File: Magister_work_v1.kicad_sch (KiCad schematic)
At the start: 0 parts

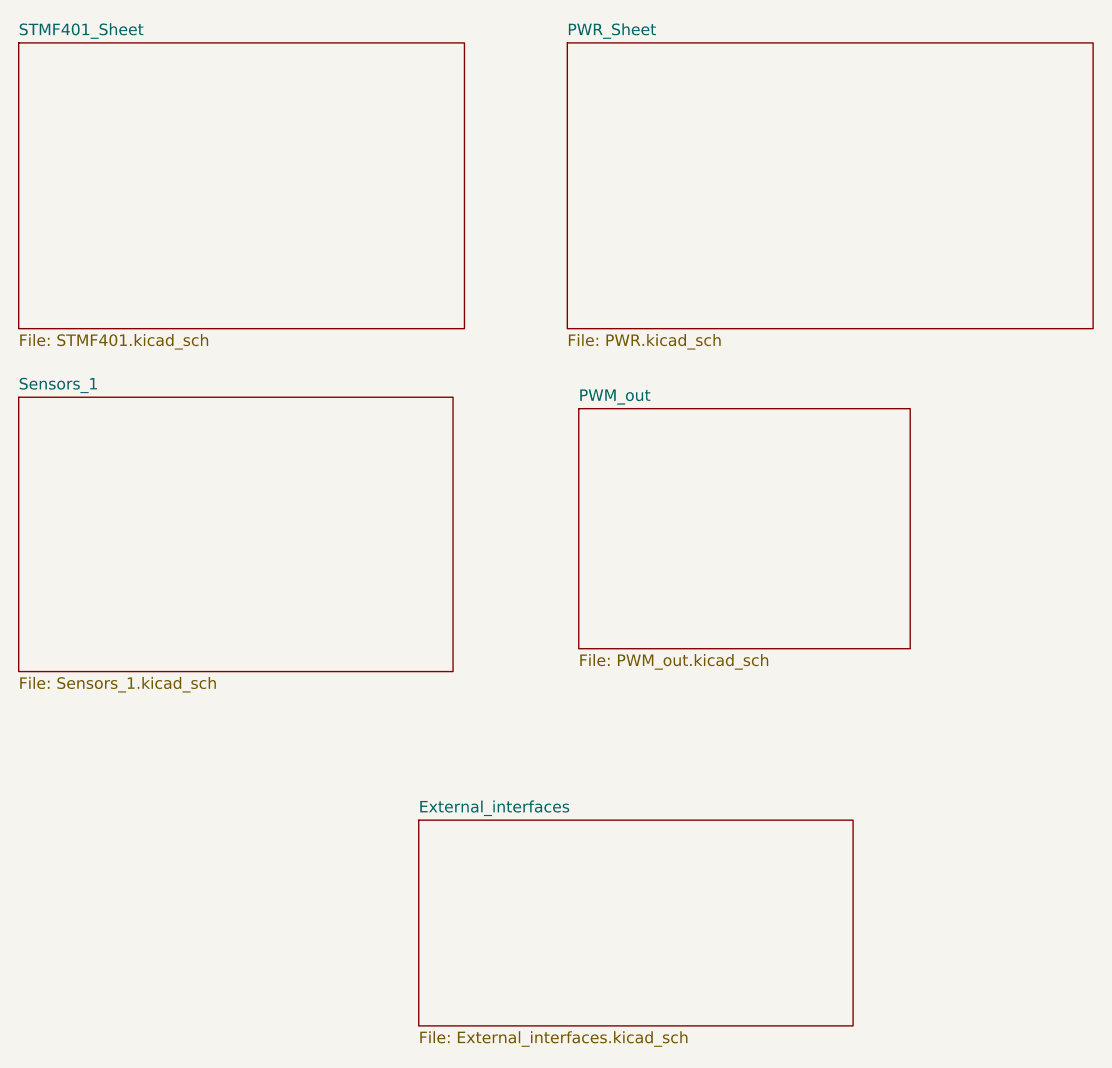
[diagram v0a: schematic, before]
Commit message: feat:убрал часть с батарейным питанием, убрал лишние элементы со старого проекта
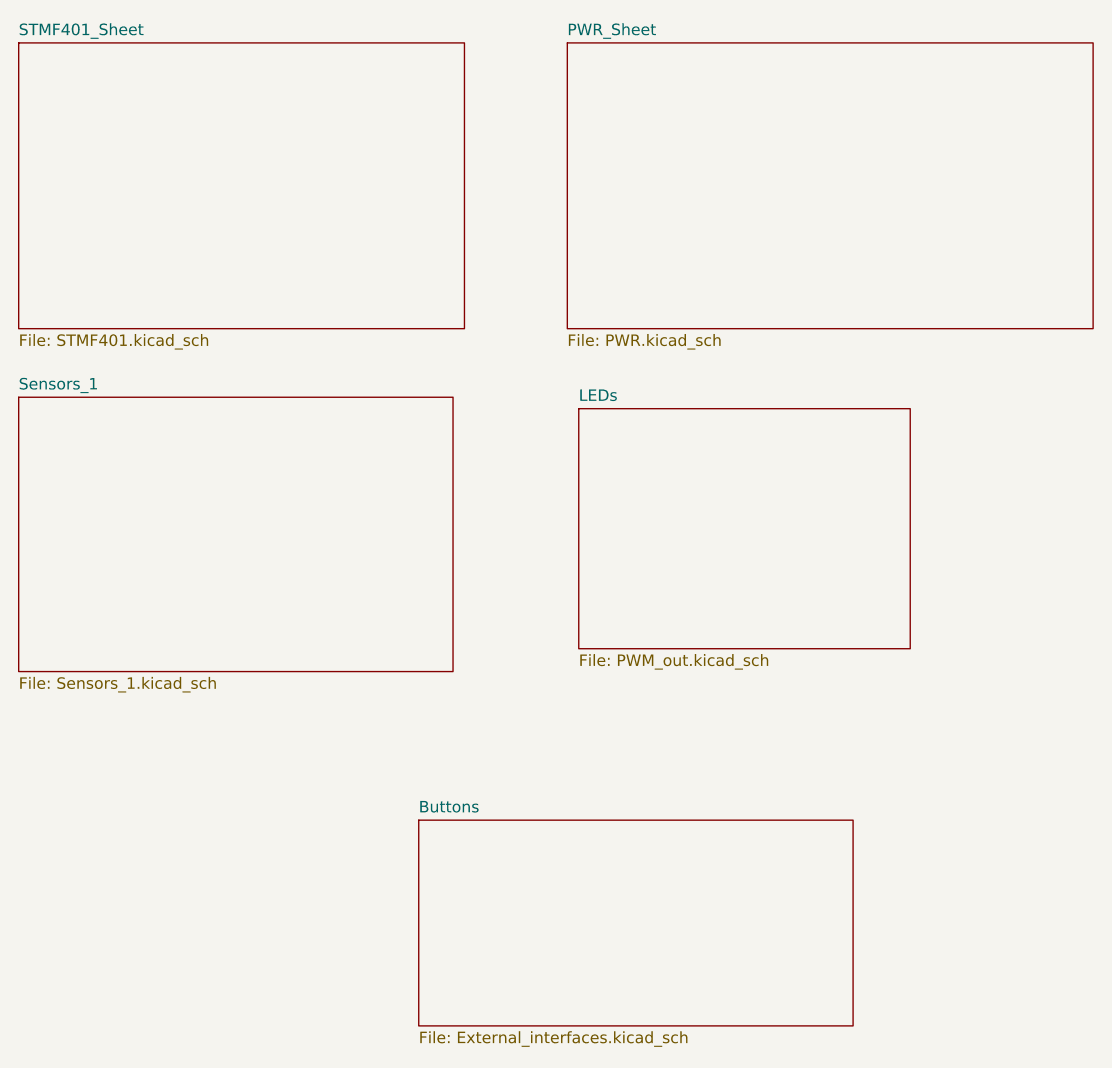
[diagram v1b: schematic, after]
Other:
- sheet External_interfaces renamed Buttons
- sheet PWM_out renamed LEDs
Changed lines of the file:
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@@
 			(color 0 0 0 0)
 		)
-		(property "Sheetname" "External_interfaces"
+		(property "Sheetname" "Buttons"
 			(at 87.63 119.9384 0)
 			(show_name no)
@@
 			(color 0 0 0 0)
 		)
-		(property "Sheetname" "PWM_out"
+		(property "Sheetname" "LEDs"
 			(at 105.41 74.2184 0)
 			(show_name no)
